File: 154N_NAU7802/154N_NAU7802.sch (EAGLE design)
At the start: 23 parts, among them J4 1725698, J5 1725698, U3 NAU7802, U4 LMV324

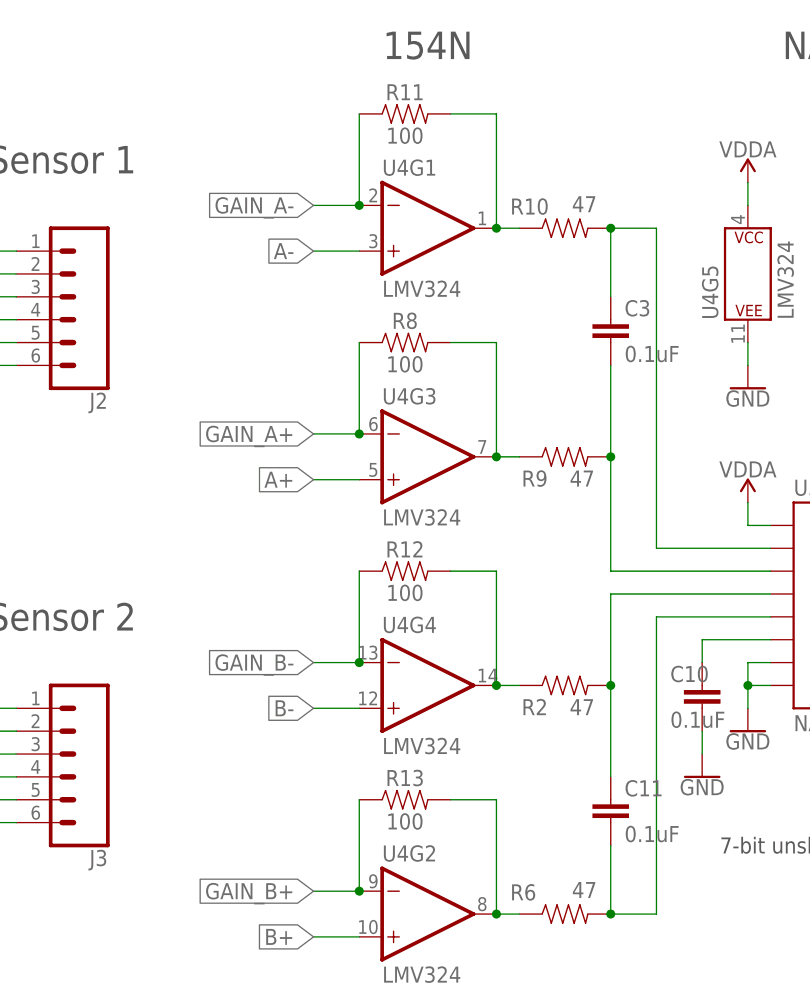
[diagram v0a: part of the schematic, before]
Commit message: Wheatstone ordered
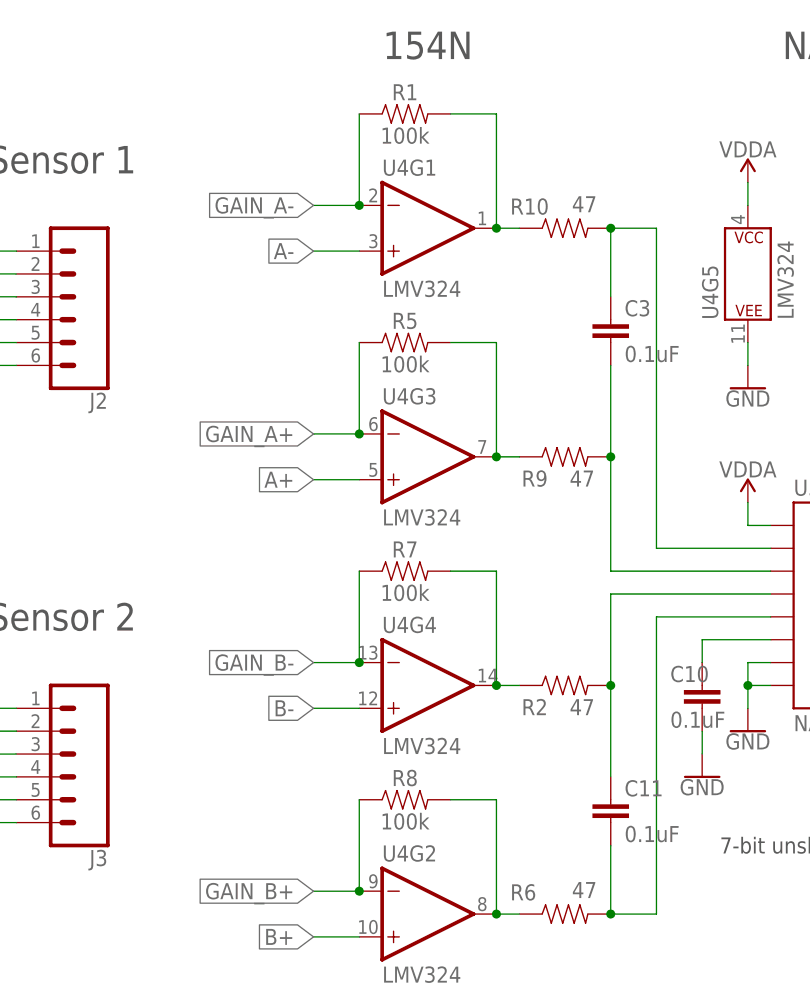
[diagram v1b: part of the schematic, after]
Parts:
- removed R11, R12, R13: 100, SparkFun-Resistors:100OHM-0603-1/10W-1%
- added R1, R5, R7: 100k, SparkFun-Resistors:100KOHM-0603-1/10W-1%
- R8: value 100 -> 100k; device SparkFun-Resistors:100OHM-0603-1/10W-1% -> SparkFun-Resistors:100KOHM-0603-1/10W-1%
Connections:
- net GAIN_A+: now also R5.1; no longer R8.1
- net GAIN_A-: now also R1.1; no longer R11.1
- net GAIN_B+: now also R8.1; no longer R13.1
- net GAIN_B-: now also R7.1; no longer R12.1
- net N$1: now also R8.2; no longer R13.2
- net N$10: now also R5.2; no longer R8.2
- net N$6: now also R7.2; no longer R12.2
- net N$9: now also R1.2; no longer R11.2
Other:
- moved on the sheet: R8
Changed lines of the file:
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@@
 <part name="C3" library="SparkFun-Capacitors" library_urn="urn:adsk.eagle:library:510" deviceset="0.1UF" device="-0603-25V-(+80/-20%)" package3d_urn="urn:adsk.eagle:package:37414/1" value="0.1uF"/>
 <part name="C11" library="SparkFun-Capacitors" library_urn="urn:adsk.eagle:library:510" deviceset="0.1UF" device="-0603-25V-(+80/-20%)" package3d_urn="urn:adsk.eagle:package:37414/1" value="0.1uF"/>
-<part name="R8" library="SparkFun-Resistors" library_urn="urn:adsk.eagle:library:532" deviceset="100OHM" device="-0603-1/10W-1%" package3d_urn="urn:adsk.eagle:package:39650/1" value="100"/>
-<part name="R11" library="SparkFun-Resistors" library_urn="urn:adsk.eagle:library:532" deviceset="100OHM" device="-0603-1/10W-1%" package3d_urn="urn:adsk.eagle:package:39650/1" value="100"/>
-<part name="R12" library="SparkFun-Resistors" library_urn="urn:adsk.eagle:library:532" deviceset="100OHM" device="-0603-1/10W-1%" package3d_urn="urn:adsk.eagle:package:39650/1" value="100"/>
-<part name="R13" library="SparkFun-Resistors" library_urn="urn:adsk.eagle:library:532" deviceset="100OHM" device="-0603-1/10W-1%" package3d_urn="urn:adsk.eagle:package:39650/1" value="100"/>
-<part name="U4" library="154N_NAU7802" deviceset="SPARKFUN-IC-AMPLIFIERS_LMV324" device="" override_package3d_urn="urn:adsk.eagle:package:24850255/2" override_package_urn="urn:adsk.eagle:footprint:24850256/1" value="LMV324"/>
+<part name="U4" library="154N_NAU7802" deviceset="SPARKFUN-IC-AMPLIFIERS_LMV324" device="" override_package3d_urn="urn:adsk.eagle:package:24850255/4" override_package_urn="urn:adsk.eagle:footprint:24850256/1" value="LMV324"/>
 <part name="J2" library="SparkFun-Connectors" library_urn="urn:adsk.eagle:library:513" deviceset="CONN_06" device="SILK_FEMALE_PTH" package3d_urn="urn:adsk.eagle:package:38009/1"/>
 <part name="J3" library="SparkFun-Connectors" library_urn="urn:adsk.eagle:library:513" deviceset="CONN_06" device="SILK_FEMALE_PTH" package3d_urn="urn:adsk.eagle:package:38009/1"/>
@@
 <part name="J5" library="1725698" deviceset="1725698" device=""/>
 <part name="J4" library="1725698" deviceset="1725698" device=""/>
+<part name="R1" library="SparkFun-Resistors" library_urn="urn:adsk.eagle:library:532" deviceset="100KOHM" device="-0603-1/10W-1%" package3d_urn="urn:adsk.eagle:package:39650/1" value="100k"/>
+<part name="R5" library="SparkFun-Resistors" library_urn="urn:adsk.eagle:library:532" deviceset="100KOHM" device="-0603-1/10W-1%" package3d_urn="urn:adsk.eagle:package:39650/1" value="100k"/>
+<part name="R7" library="SparkFun-Resistors" library_urn="urn:adsk.eagle:library:532" deviceset="100KOHM" device="-0603-1/10W-1%" package3d_urn="urn:adsk.eagle:package:39650/1" value="100k"/>
+<part name="R8" library="SparkFun-Resistors" library_urn="urn:adsk.eagle:library:532" deviceset="100KOHM" device="-0603-1/10W-1%" package3d_urn="urn:adsk.eagle:package:39650/1" value="100k"/>
 </parts>
 <sheets>
@@
 <attribute name="VALUE" x="52.324" y="25.781" size="1.778" layer="96" font="vector"/>
 </instance>
-<instance part="R8" gate="G$1" x="27.94" y="81.28" smashed="yes">
-<attribute name="NAME" x="27.94" y="82.804" size="1.778" layer="95" font="vector" align="bottom-center"/>
-<attribute name="VALUE" x="27.94" y="79.756" size="1.778" layer="96" font="vector" align="top-center"/>
-</instance>
-<instance part="R11" gate="G$1" x="27.94" y="106.68" smashed="yes">
-<attribute name="NAME" x="27.94" y="108.204" size="1.778" layer="95" font="vector" align="bottom-center"/>
-<attribute name="VALUE" x="27.94" y="105.156" size="1.778" layer="96" font="vector" align="top-center"/>
-</instance>
-<instance part="R12" gate="G$1" x="27.94" y="55.88" smashed="yes">
-<attribute name="NAME" x="27.94" y="57.404" size="1.778" layer="95" font="vector" align="bottom-center"/>
-<attribute name="VALUE" x="27.94" y="54.356" size="1.778" layer="96" font="vector" align="top-center"/>
-</instance>
-<instance part="R13" gate="G$1" x="27.94" y="30.48" smashed="yes">
-<attribute name="NAME" x="27.94" y="32.004" size="1.778" layer="95" font="vector" align="bottom-center"/>
-<attribute name="VALUE" x="27.94" y="28.956" size="1.778" layer="96" font="vector" align="top-center"/>
-</instance>
 <instance part="U4" gate="G1" x="30.48" y="93.98" smashed="yes">
 <attribute name="NAME" x="25.4" y="99.822" size="1.778" layer="95" font="vector"/>
@@
 <attribute name="NAME" x="-44.45" y="48.26" size="1.778" layer="95" align="center-left"/>
 <attribute name="VALUE" x="-44.45" y="45.72" size="1.778" layer="96" align="center-left"/>
+</instance>
+<instance part="R1" gate="G$1" x="27.94" y="106.68" smashed="yes">
+<attribute name="NAME" x="27.94" y="108.204" size="1.778" layer="95" font="vector" align="bottom-center"/>
+<attribute name="VALUE" x="27.94" y="105.156" size="1.778" layer="96" font="vector" align="top-center"/>
+</instance>
+<instance part="R5" gate="G$1" x="27.94" y="81.28" smashed="yes">
+<attribute name="NAME" x="27.94" y="82.804" size="1.778" layer="95" font="vector" align="bottom-center"/>
+<attribute name="VALUE" x="27.94" y="79.756" size="1.778" layer="96" font="vector" align="top-center"/>
+</instance>
+<instance part="R7" gate="G$1" x="27.94" y="55.88" smashed="yes">
+<attribute name="NAME" x="27.94" y="57.404" size="1.778" layer="95" font="vector" align="bottom-center"/>
+<attribute name="VALUE" x="27.94" y="54.356" size="1.778" layer="96" font="vector" align="top-center"/>
+</instance>
+<instance part="R8" gate="G$1" x="27.94" y="30.48" smashed="yes">
+<attribute name="NAME" x="27.94" y="32.004" size="1.778" layer="95" font="vector" align="bottom-center"/>
+<attribute name="VALUE" x="27.94" y="28.956" size="1.778" layer="96" font="vector" align="top-center"/>
 </instance>
 </instances>
@@
 <pinref part="U4" gate="G3" pin="-IN"/>
 <label x="17.78" y="71.12" size="1.778" layer="95" rot="R180" xref="yes"/>
-<pinref part="R8" gate="G$1" pin="1"/>
 <wire x1="22.86" y1="71.12" x2="22.86" y2="81.28" width="0.1524" layer="91"/>
 <junction x="22.86" y="71.12"/>
+<pinref part="R5" gate="G$1" pin="1"/>
 </segment>
 <segment>
@@
 <pinref part="U4" gate="G4" pin="-IN"/>
 <label x="17.78" y="45.72" size="1.778" layer="95" rot="R180" xref="yes"/>
-<pinref part="R12" gate="G$1" pin="1"/>
 <wire x1="22.86" y1="45.72" x2="22.86" y2="55.88" width="0.1524" layer="91"/>
 <junction x="22.86" y="45.72"/>
+<pinref part="R7" gate="G$1" pin="1"/>
 </segment>
 <segment>
@@
 <wire x1="22.86" y1="20.32" x2="17.78" y2="20.32" width="0.1524" layer="91"/>
 <label x="17.78" y="20.32" size="1.778" layer="95" rot="R180" xref="yes"/>
-<pinref part="R13" gate="G$1" pin="1"/>
 <wire x1="22.86" y1="20.32" x2="22.86" y2="30.48" width="0.1524" layer="91"/>
 <junction x="22.86" y="20.32"/>
+<pinref part="R8" gate="G$1" pin="1"/>
 </segment>
 <segment>
@@
 <segment>
 <pinref part="U4" gate="G2" pin="OUT"/>
-<pinref part="R13" gate="G$1" pin="2"/>
 <wire x1="38.1" y1="17.78" x2="38.1" y2="30.48" width="0.1524" layer="91"/>
 <wire x1="38.1" y1="30.48" x2="33.02" y2="30.48" width="0.1524" layer="91"/>
@@
 <wire x1="40.64" y1="17.78" x2="38.1" y2="17.78" width="0.1524" layer="91"/>
 <junction x="38.1" y="17.78"/>
+<pinref part="R8" gate="G$1" pin="2"/>
 </segment>
 </net>
@@
 <segment>
 <pinref part="U4" gate="G4" pin="OUT"/>
-<pinref part="R12" gate="G$1" pin="2"/>
 <wire x1="38.1" y1="43.18" x2="38.1" y2="55.88" width="0.1524" layer="91"/>
 <wire x1="38.1" y1="55.88" x2="33.02" y2="55.88" width="0.1524" layer="91"/>
@@
 <wire x1="40.64" y1="43.18" x2="38.1" y2="43.18" width="0.1524" layer="91"/>
 <junction x="38.1" y="43.18"/>
+<pinref part="R7" gate="G$1" pin="2"/>
 </segment>
 </net>
@@
 <segment>
 <pinref part="U4" gate="G1" pin="OUT"/>
-<pinref part="R11" gate="G$1" pin="2"/>
 <wire x1="38.1" y1="93.98" x2="38.1" y2="106.68" width="0.1524" layer="91"/>
 <wire x1="38.1" y1="106.68" x2="33.02" y2="106.68" width="0.1524" layer="91"/>
@@
 <wire x1="40.64" y1="93.98" x2="38.1" y2="93.98" width="0.1524" layer="91"/>
 <junction x="38.1" y="93.98"/>
+<pinref part="R1" gate="G$1" pin="2"/>
 </segment>
 </net>
@@
 <segment>
 <pinref part="U4" gate="G3" pin="OUT"/>
-<pinref part="R8" gate="G$1" pin="2"/>
 <wire x1="38.1" y1="68.58" x2="38.1" y2="81.28" width="0.1524" layer="91"/>
 <wire x1="38.1" y1="81.28" x2="33.02" y2="81.28" width="0.1524" layer="91"/>
@@
 <wire x1="40.64" y1="68.58" x2="38.1" y2="68.58" width="0.1524" layer="91"/>
 <junction x="38.1" y="68.58"/>
+<pinref part="R5" gate="G$1" pin="2"/>
 </segment>
 </net>
@@
 <wire x1="22.86" y1="96.52" x2="17.78" y2="96.52" width="0.1524" layer="91"/>
 <label x="17.78" y="96.52" size="1.778" layer="95" rot="R180" xref="yes"/>
-<pinref part="R11" gate="G$1" pin="1"/>
 <wire x1="22.86" y1="96.52" x2="22.86" y2="106.68" width="0.1524" layer="91"/>
 <junction x="22.86" y="96.52"/>
-</segment>
-<segment>
+<pinref part="R1" gate="G$1" pin="1"/>
+</segment>
+<segment>

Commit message: John
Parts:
- added C1: 1.0uF, SparkFun-Capacitors:1.0UF-0603-16V-10%
- added IC1: MCP604SL, linear:MCP604SL
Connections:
- net 3.3V: now also C1.1, IC1P.V+, U4G5.P$V+
- net GND: now also C1.2, IC1P.V-
- net VDDA: no longer U4G5.P$V+
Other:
- moved on the sheet: C12, C9, J4, J5

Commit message: Lagopus 3.0 order
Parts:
- added IC2: NAU7802SGI, NAU7802SGI:NAU7802SGI
- added RN1: CAY16-1003F4LF, CAY16-1003F4LF:CAY16-1003F4LF
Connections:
- new net N$16: IC1C.OUT, IC2.VIN2P, RN1.R3_2
- new net N$5: IC1A.OUT, IC2.VIN1N, RN1.R1_2
- new net N$7: IC1B.OUT, IC2.VIN1P, RN1.R2_2
- new net N$8: IC1D.OUT, IC2.VIN2N, RN1.R4_2
- net A+: now also IC1B.+IN
- net A-: now also IC1A.+IN
- net B+: now also IC1C.+IN
- net B-: now also IC1D.+IN
- net GAIN_A+: now also IC1B.-IN, RN1.R2_1
- net GAIN_A-: now also IC1A.-IN, RN1.R1_1
- net GAIN_B+: now also IC1C.-IN, RN1.R3_1
- net GAIN_B-: now also IC1D.-IN, RN1.R4_1
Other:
- moved on the sheet: IC1A, IC1B, IC1C, IC1D
